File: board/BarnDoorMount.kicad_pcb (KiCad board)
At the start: 4 copper layers, 51.1 x 33 mm, 33 parts, among them Q1 PZT2222A, Q2 PZT2222A, U1 MSP430FR2433, U2 LM317, U3 A3967

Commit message: Revision 2 of the driver board
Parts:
- removed Battery: Battery, Connector_PinHeader_2.54mm:PinHeader_1x02_P2.54mm_Vertical
- removed Camera: Shutter Control, Connector_PinHeader_2.54mm:PinHeader_1x04_P2.54mm_Vertical
- removed Debug: SBW, Connector_PinHeader_2.54mm:PinHeader_1x02_P2.54mm_Vertical
- removed Display: LCD, Connector_PinHeader_2.54mm:PinHeader_1x08_P2.54mm_Vertical
- removed Stepper Motor: Stepper Motor, Connector_PinHeader_2.54mm:PinHeader_1x04_P2.54mm_Vertical
- added J1: SBW, Connector_JST:JST_XH_B04B-XH-A_1x04_P2.50mm_Vertical, F.Cu at (160.3, 108.5)
- added J2: Shutter Control, Connector_JST:JST_XH_B04B-XH-A_1x04_P2.50mm_Vertical, F.Cu at (167.4, 86.6)
- added J3: LCD, Connector_JST:JST_XH_B08B-XH-A_1x08_P2.50mm_Vertical, F.Cu at (121.7, 91.7)
- added J4: Battery, Connector_JST:JST_XH_B02B-XH-A_1x02_P2.50mm_Vertical, F.Cu at (167.4, 78.2)
- added J5: Stepper Motor, Connector_JST:JST_XH_B04B-XH-A_1x04_P2.50mm_Vertical, F.Cu at (167.4, 100.1)
- added R16: 10K, Resistor_SMD:R_0603_1608Metric_Pad1.05x0.95mm_HandSolder, F.Cu at (149.1, 95.2)
- added R17: 10K, Resistor_SMD:R_0603_1608Metric_Pad1.05x0.95mm_HandSolder, F.Cu at (149.1, 97.0)
- added R18: 10K, Resistor_SMD:R_0603_1608Metric_Pad1.05x0.95mm_HandSolder, F.Cu at (136.1, 91.4)
- added R19: 10K, Resistor_SMD:R_0603_1608Metric_Pad1.05x0.95mm_HandSolder, F.Cu at (136.1, 75.7)
- added R20: 10K, Resistor_SMD:R_0603_1608Metric_Pad1.05x0.95mm_HandSolder, F.Cu at (142.0, 73.7)
- added R21: JUMPER, Resistor_SMD:R_0603_1608Metric_Pad1.05x0.95mm_HandSolder, F.Cu at (161.5, 72.6)
- added R22: JUMPER, Resistor_SMD:R_0603_1608Metric_Pad1.05x0.95mm_HandSolder, F.Cu at (158.0, 72.6)
- added R23: 390, Resistor_SMD:R_0603_1608Metric_Pad1.05x0.95mm_HandSolder, F.Cu at (126.5, 77.0)
- added SW1: SELECT, Button_Switch_SMD:SW_SPST_B3S-1100, F.Cu at (123.2, 106.4)
- added SW2: OK, Button_Switch_SMD:SW_SPST_B3S-1100, F.Cu at (134.9, 106.4)
- added TP1: TP_GND, TestPoint:TestPoint_Pad_D2.0mm, F.Cu at (165.9, 73.2)
- added TP2: TP_33V, TestPoint:TestPoint_Pad_D2.0mm, F.Cu at (169.9, 73.2)
- + C5: renamed from C5
- C2 +: renamed from C2
- moved R1 5.14 mm to (149.1, 101.1), turned to 180 degrees
- moved C1 2.27 mm to (149.1, 99.3), turned to 0 degrees
- moved C2 + 0.92 mm to (142.5, 102.1)
- moved C3 0.92 mm to (142.5, 103.9)
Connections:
- R14 pad 1: +3V3 -> Net-(R14-Pad1)
- U1 pad 21: Net-(U1-Pad21) -> SELECT_BTN
- U1 pad 22: Net-(U1-Pad22) -> OK_BTN
- U2 pad 2: +3V3 -> Net-(R14-Pad1)
- U3 pad 15: +3V3 -> Net-(R20-Pad2)
- U3 pad 22: +3V3 -> Net-(R19-Pad2)
- U3 pad 3: +3V3 -> Net-(R18-Pad2)
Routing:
- net GND: track 53.0 -> 85.9 mm, vias 13 -> 15
- net Net-(R23-Pad1): track 0.00 -> 29.8 mm, vias 0 -> 2
- net SELECT_BTN: track 0.00 -> 23.1 mm
- net +3V3: track 38.6 -> 18.7 mm
- net Net-(R14-Pad1): track 0.00 -> 16.0 mm, vias 0 -> 1
- net OK_BTN: track 0.00 -> 12.6 mm
- net Net-(J1-Pad3): track 7.20 -> 18.0 mm, vias 2 -> 1
- net Net-(J3-Pad5): track 23.2 -> 32.5 mm
- net Net-(J3-Pad4): track 23.2 -> 31.5 mm
- net Net-(J4-Pad1): track 0.00 -> 7.79 mm
- net Net-(C1-Pad1): track 10.1 -> 17.5 mm
- net Net-(J3-Pad6): track 25.3 -> 32.2 mm, vias 2 -> 0
- net Net-(R20-Pad2): track 0.00 -> 6.77 mm
- net Net-(J3-Pad7): track 27.3 -> 33.7 mm, vias 2 -> 0
- net Net-(J3-Pad8): track 0.00 -> 5.68 mm
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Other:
- board size 51.1 x 33 mm -> 54.9 x 41.4 mm
- board text added: "+ Batt -"
- board text added: "Astrophotography Camera Mount Controller"
- board text added: "Debug"
- board text added: "OK"
- board text added: "Pwr"
- board text added: "Rev 2"
- board text added: "SEL"
- board text added: "Shutter Control"
- board text added: "Stepper Motor"
- board text removed: "Barn Door Camera Mount Controller"
- board text removed: "Rev 1"

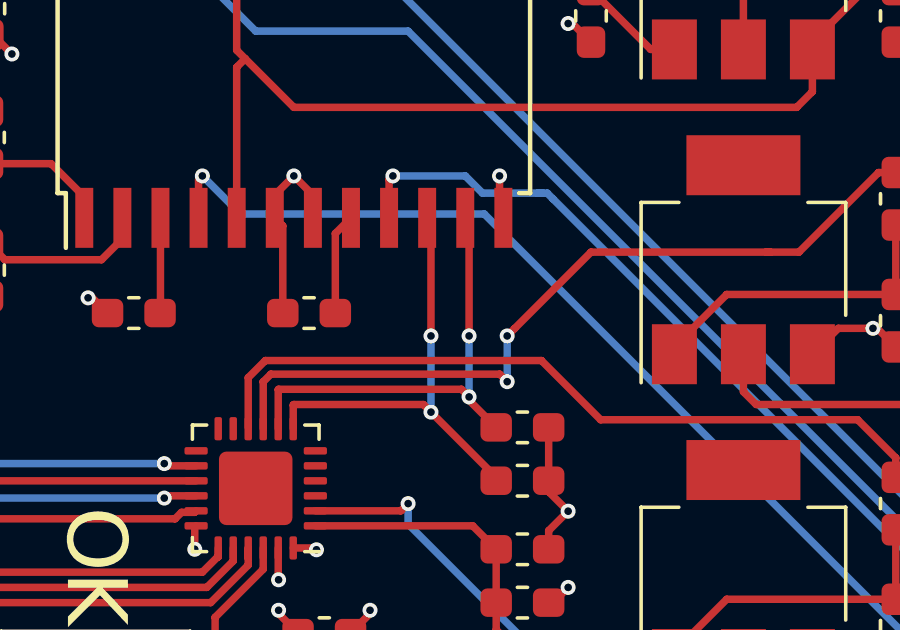
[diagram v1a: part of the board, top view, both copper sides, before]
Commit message: Board changes for rev 3: swap STEP and DIR pins between the MCU and stepper driver
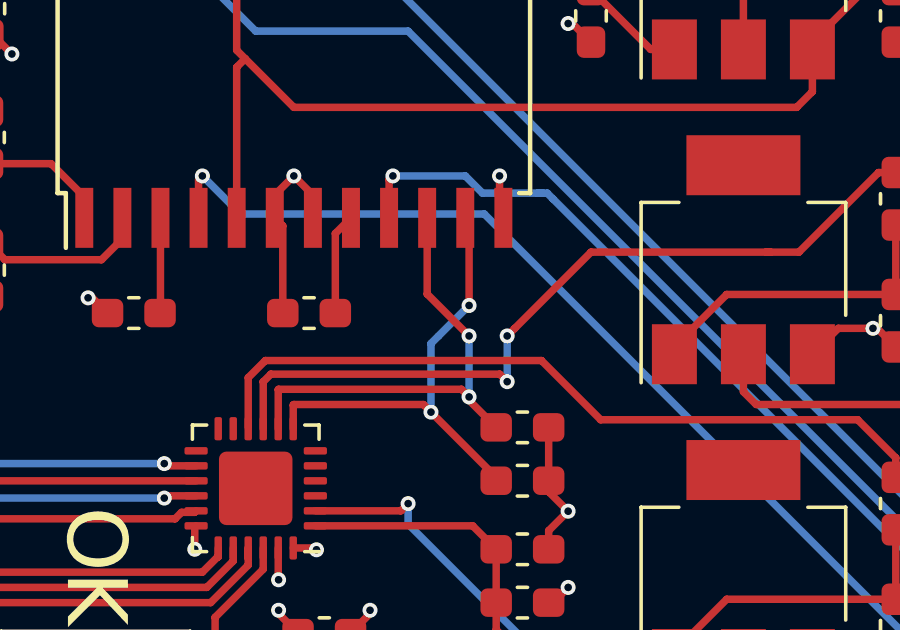
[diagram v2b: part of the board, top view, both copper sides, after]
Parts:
- C2: renamed from C2 +
- C5: renamed from + C5
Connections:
- U3 pad 10: Net-(R17-Pad1) -> Net-(R16-Pad1)
- U3 pad 11: Net-(R16-Pad1) -> Net-(R17-Pad1)
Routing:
- net Net-(R16-Pad1): track 15.2 -> 15.9 mm
- net Net-(R17-Pad1): track 15.2 -> 15.7 mm
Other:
- board text added: "+"
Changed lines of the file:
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@@
   (general
     (thickness 1.6)
-    (drawings 27)
-    (tracks 355)
+    (drawings 29)
+    (tracks 358)
     (zones 0)
     (modules 45)
@@
   (page A4)
   (layers
-    (0 F.Cu signal hide)
+    (0 F.Cu signal)
     (1 In1.Cu power hide)
     (2 In2.Cu power hide)
-    (31 B.Cu signal hide)
+    (31 B.Cu signal)
     (33 F.Adhes user hide)
     (35 F.Paste user hide)
@@
       (net 3 +3V3))
     (pad 11 smd rect (at -4.7 5.715 90) (size 2 0.6) (layers F.Cu F.Paste F.Mask)
+      (net 40 "Net-(R17-Pad1)"))
+    (pad 10 smd rect (at -4.7 4.445 90) (size 2 0.6) (layers F.Cu F.Paste F.Mask)
       (net 39 "Net-(R16-Pad1)"))
-    (pad 10 smd rect (at -4.7 4.445 90) (size 2 0.6) (layers F.Cu F.Paste F.Mask)
-      (net 40 "Net-(R17-Pad1)"))
     (pad 9 smd rect (at -4.7 3.175 90) (size 2 0.6) (layers F.Cu F.Paste F.Mask)
       (net 17 "Net-(J5-Pad3)"))
@@
     (tags "capacitor handsolder")
     (attr smd)
-    (fp_text reference "C2 +" (at 0 1.27 180) (layer Dwgs.User)
+    (fp_text reference C2 (at 0 1.27 180) (layer Dwgs.User)
       (effects (font (size 0.75 0.75) (thickness 0.15)))
     )
@@
     (tags "capacitor handsolder")
     (attr smd)
-    (fp_text reference "+ C5" (at 0 1.524 90) (layer Dwgs.User)
+    (fp_text reference C5 (at 0.762 1.524 90) (layer Dwgs.User)
       (effects (font (size 0.8 0.8) (thickness 0.15)))
     )
@@
       (rotate (xyz 0 0 0))
     )
+  )
+  (gr_text + (at 163.068 78.486) (layer Dwgs.User)
+    (effects (font (size 0.75 0.75) (thickness 0.1875)))
+  )
+  (gr_text + (at 144.78 102.108) (layer Dwgs.User)
+    (effects (font (size 0.75 0.75) (thickness 0.1875)))
   )
   (gr_text OK (at 134.874 101.854 270) (layer F.SilkS)
@@
   (segment (start 140.958 93.992) (end 140.97 93.98) (width 0.25) (layer F.Cu) (net 39))
   (segment (start 147.32 94.234) (end 147.32 92.202) (width 0.25) (layer B.Cu) (net 39))
-  (segment (start 147.32 88.393) (end 147.193 88.266) (width 0.25) (layer F.Cu) (net 39))
-  (segment (start 147.32 92.202) (end 147.32 88.393) (width 0.25) (layer F.Cu) (net 39))
   (segment (start 147.32 94.347) (end 148.223 95.25) (width 0.25) (layer F.Cu) (net 39))
   (segment (start 147.32 94.234) (end 147.32 94.347) (width 0.25) (layer F.Cu) (net 39))
-  (via (at 146.05 92.202) (size 0.5) (drill 0.254) (layers F.Cu B.Cu) (net 40))
-  (via (at 146.05 94.742) (size 0.5) (drill 0.254) (layers F.Cu B.Cu) (net 40))
   (segment (start 145.796 94.488) (end 146.05 94.742) (width 0.25) (layer F.Cu) (net 40))
   (segment (start 141.478 94.488) (end 145.796 94.488) (width 0.25) (layer F.Cu) (net 40))
   (segment (start 141.458 95.2945) (end 141.458 94.508) (width 0.25) (layer F.Cu) (net 40))
   (segment (start 141.458 94.508) (end 141.478 94.488) (width 0.25) (layer F.Cu) (net 40))
-  (segment (start 146.05 92.202) (end 146.05 94.742) (width 0.25) (layer B.Cu) (net 40))
-  (segment (start 146.05 88.393) (end 145.923 88.266) (width 0.25) (layer F.Cu) (net 40))
-  (segment (start 146.05 92.202) (end 146.05 88.393) (width 0.25) (layer F.Cu) (net 40))
   (segment (start 148.223 96.915) (end 148.223 97.028) (width 0.25) (layer F.Cu) (net 40))
   (segment (start 146.05 94.742) (end 148.223 96.915) (width 0.25) (layer F.Cu) (net 40))
+  (segment (start 146.05 88.393) (end 145.923 88.266) (width 0.25) (layer F.Cu) (net 39))
+  (segment (start 145.923 90.805) (end 145.923 88.266) (width 0.25) (layer F.Cu) (net 39))
+  (segment (start 147.32 92.202) (end 145.923 90.805) (width 0.25) (layer F.Cu) (net 39))
+  (via (at 146.05 94.742) (size 0.5) (drill 0.254) (layers F.Cu B.Cu) (net 40))
+  (via (at 147.32 91.186) (size 0.5) (drill 0.254) (layers F.Cu B.Cu) (net 40))
+  (segment (start 146.304 92.202) (end 147.32 91.186) (width 0.25) (layer B.Cu) (net 40))
+  (segment (start 146.05 94.742) (end 146.05 92.456) (width 0.25) (layer B.Cu) (net 40))
+  (segment (start 146.05 92.456) (end 146.304 92.202) (width 0.25) (layer B.Cu) (net 40))
+  (segment (start 147.32 88.393) (end 147.193 88.266) (width 0.25) (layer F.Cu) (net 40))
+  (segment (start 147.32 91.186) (end 147.32 88.393) (width 0.25) (layer F.Cu) (net 40))
   (segment (start 137.033 91.426) (end 137.019 91.44) (width 0.25) (layer F.Cu) (net 41))
   (segment (start 137.033 88.266) (end 137.033 91.426) (width 0.25) (layer F.Cu) (net 41))
